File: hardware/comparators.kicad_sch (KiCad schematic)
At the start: 108 parts, among them J35 SMA, J36 SMA, J37 SMA, J38 SMA, J39 SMA, J40 SMA, J41 SMA, J42 SMA, J43 SMA, J44 SMA, J45 SMA, J46 SMA, J47 SMA, J48 SMA, J49 SMA, J50 SMA, J51 SMA, J52 SMA, J53 SMA, J54 SMA, J55 SMA, J56 SMA, J57 SMA, J58 SMA, SW7 SW_DIP_x03, U31 TXB0108PW, U32 TLV3502AIDR, U33 TLV3502AIDR, U34 TLV3502AIDR, U35 TLV3502AIDR, U36 TXB0108PW, U37 TLV3502AIDR, U38 TLV3502AIDR, U39 TLV3502AIDR, U40 TLV3502AIDR, U41 TXB0108PW, U42 TLV3502AIDR, U43 TLV3502AIDR, U44 TLV3502AIDR, U45 TLV3502AIDR

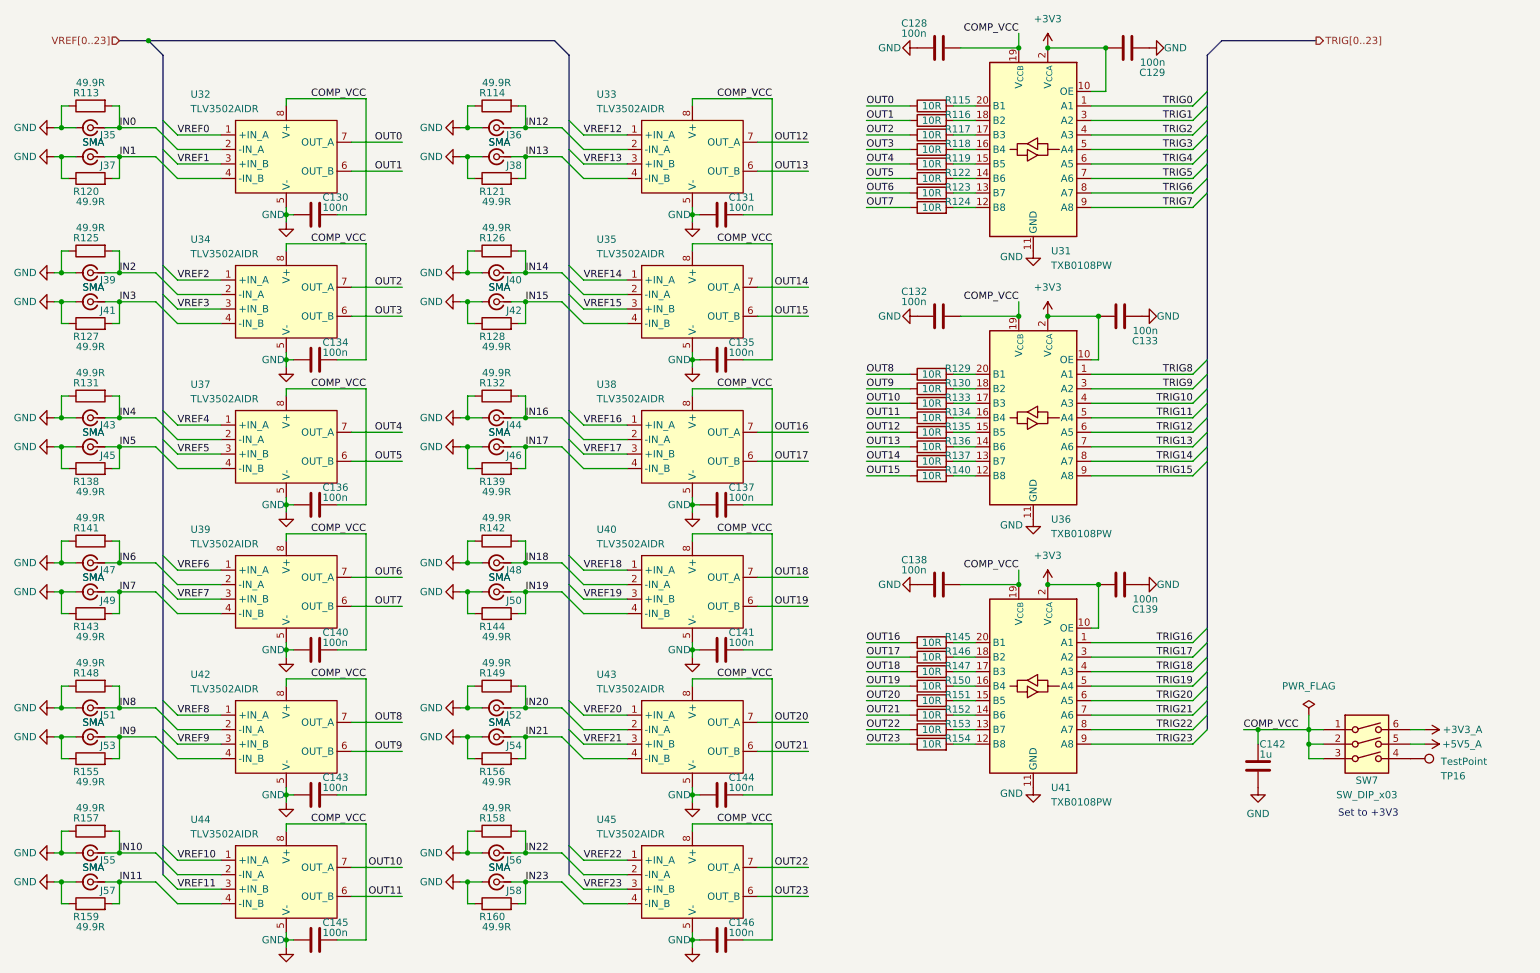
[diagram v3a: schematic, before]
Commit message: route digital inputs
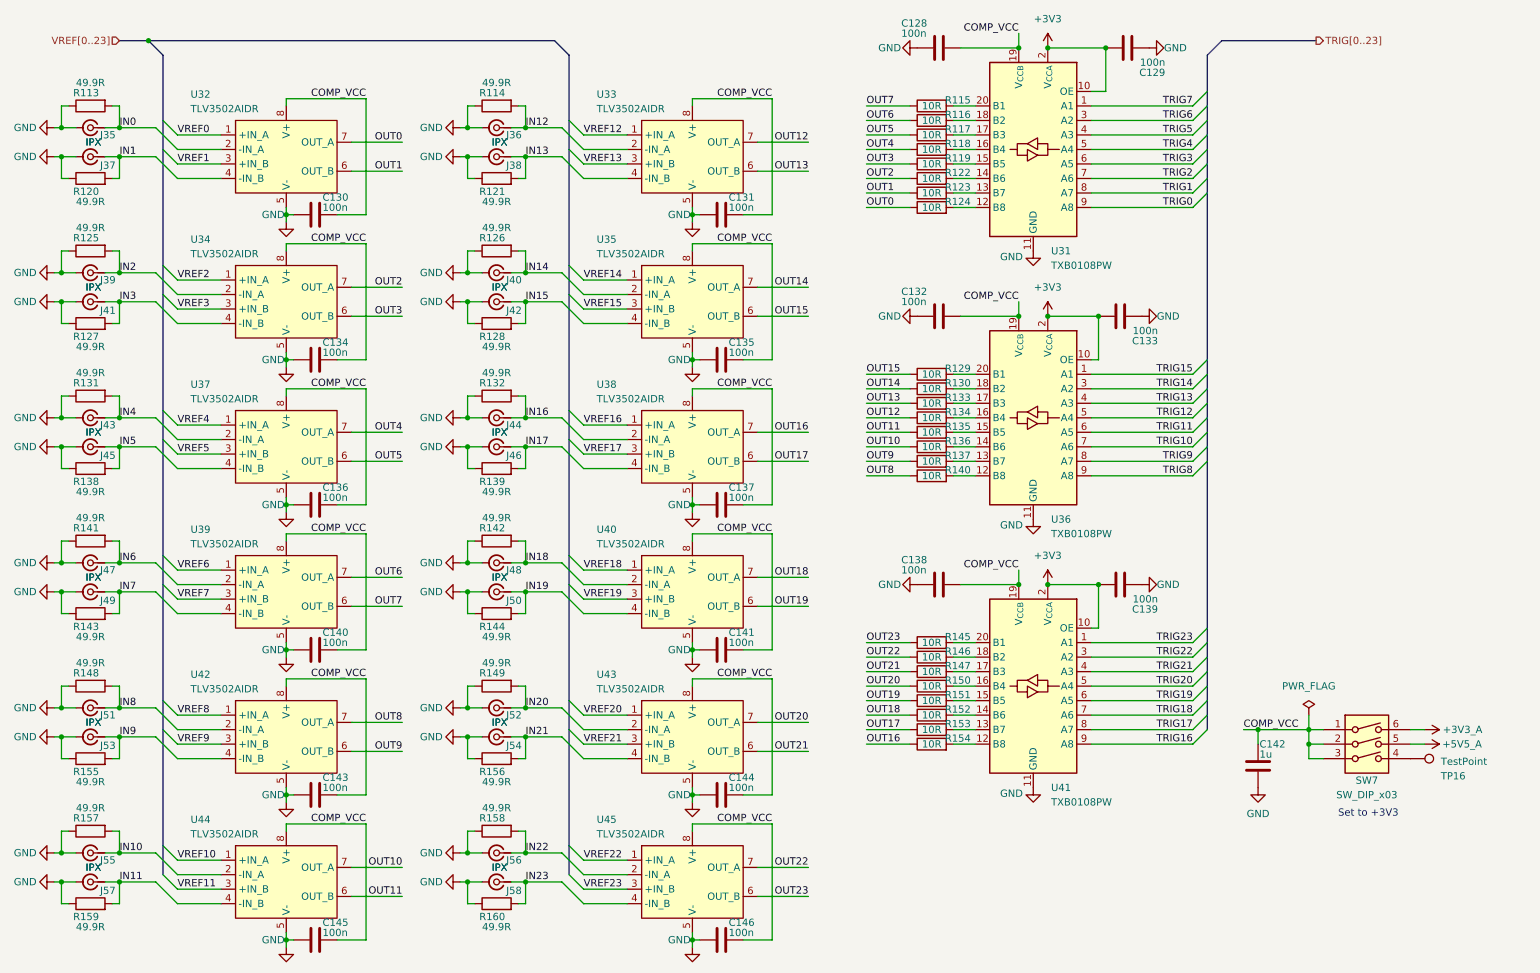
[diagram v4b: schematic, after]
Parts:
- J35, J36, J37, J38, J39, J40, J41, J42, J43, J44, J45, J46, J47, J48, J49, J50, J51, J52, J53, J54, J55, J56, J57, J58: value SMA -> IPX; footprint Connector_Coaxial:SMA_Amphenol_901-144_Vertical -> digital:BWIPX-1-001E
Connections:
- net OUT0: now also R124.1; no longer R115.1
- net OUT1: now also R123.1; no longer R116.1
- net OUT10: now also R136.1; no longer R133.1
- net OUT11: now also R135.1; no longer R134.1
- net OUT12: now also R134.1; no longer R135.1
- net OUT13: now also R133.1; no longer R136.1
- net OUT14: now also R130.1; no longer R137.1
- net OUT15: now also R129.1; no longer R140.1
- net OUT16: now also R154.1; no longer R145.1
- net OUT17: now also R153.1; no longer R146.1
- net OUT18: now also R152.1; no longer R147.1
- net OUT19: now also R151.1; no longer R150.1
- net OUT2: now also R122.1; no longer R117.1
- net OUT20: now also R150.1; no longer R151.1
- net OUT21: now also R147.1; no longer R152.1
- net OUT22: now also R146.1; no longer R153.1
- net OUT23: now also R145.1; no longer R154.1
- net OUT3: now also R119.1; no longer R118.1
- net OUT4: now also R118.1; no longer R119.1
- net OUT5: now also R117.1; no longer R122.1
- net OUT6: now also R116.1; no longer R123.1
- net OUT7: now also R115.1; no longer R124.1
- net OUT8: now also R140.1; no longer R129.1
- net OUT9: now also R137.1; no longer R130.1
- net TRIG0: now also U31.9 (A8); no longer U31.1 (A1)
- net TRIG1: now also U31.8 (A7); no longer U31.3 (A2)
- net TRIG10: now also U36.7 (A6); no longer U36.4 (A3)
- net TRIG11: now also U36.6 (A5); no longer U36.5 (A4)
- net TRIG12: now also U36.5 (A4); no longer U36.6 (A5)
- net TRIG13: now also U36.4 (A3); no longer U36.7 (A6)
- net TRIG14: now also U36.3 (A2); no longer U36.8 (A7)
- net TRIG15: now also U36.1 (A1); no longer U36.9 (A8)
- net TRIG16: now also U41.9 (A8); no longer U41.1 (A1)
- net TRIG17: now also U41.8 (A7); no longer U41.3 (A2)
- net TRIG18: now also U41.7 (A6); no longer U41.4 (A3)
- net TRIG19: now also U41.6 (A5); no longer U41.5 (A4)
- net TRIG2: now also U31.7 (A6); no longer U31.4 (A3)
- net TRIG20: now also U41.5 (A4); no longer U41.6 (A5)
- net TRIG21: now also U41.4 (A3); no longer U41.7 (A6)
- net TRIG22: now also U41.3 (A2); no longer U41.8 (A7)
- net TRIG23: now also U41.1 (A1); no longer U41.9 (A8)
- net TRIG3: now also U31.6 (A5); no longer U31.5 (A4)
- net TRIG4: now also U31.5 (A4); no longer U31.6 (A5)
- net TRIG5: now also U31.4 (A3); no longer U31.7 (A6)
- net TRIG6: now also U31.3 (A2); no longer U31.8 (A7)
- net TRIG7: now also U31.1 (A1); no longer U31.9 (A8)
- net TRIG8: now also U36.9 (A8); no longer U36.1 (A1)
- net TRIG9: now also U36.8 (A7); no longer U36.3 (A2)

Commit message: route more
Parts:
- removed TP16: TestPoint, TestPoint:TestPoint_Pad_D1.0mm, symbol Connector:TestPoint
- added TP17: TestPoint_Alt, digital:TestPoint_Keystone_5015_Micro_Mini, symbol Connector:TestPoint_Alt
- J35, J36, J37, J38, J39, J40, J41, J42, J43, J44, J45, J46, J47, J48, J49, J50, J51, J52, J53, J54, J55, J56, J57, J58: value IPX -> IPEX-1; LCSC (none) -> C496552
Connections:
- net at SW7.4: now also TP17.1

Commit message: route
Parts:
- renumbered C130 to C100, C131 to C101, C132 to C102, C133 to C103, C134 to C104, C135 to C105, C136 to C106, C137 to C107, C138 to C108, C139 to C109, C140 to C110, C141 to C111, C142 to C112, C143 to C113, C144 to C114, C145 to C115, C146 to C116, C128 to C98, C129 to C99, J35 to J21, J36 to J22, J37 to J23, J38 to J24, J39 to J25, J40 to J26, J41 to J27, J42 to J28, J43 to J29, J44 to J30, J45 to J31, J46 to J32, J47 to J33, J48 to J34, J49 to J35, J50 to J36, J51 to J37, J52 to J38, J53 to J39, J54 to J40, J55 to J41, J56 to J42, J57 to J43, J58 to J44, R124 to R100, R125 to R101, R126 to R102, R127 to R103, R128 to R104, R129 to R105, R130 to R106, R131 to R107, R132 to R108, R133 to R109, R134 to R110, R135 to R111, R136 to R112, R137 to R113, R138 to R114, R139 to R115, R140 to R116, R141 to R117, R142 to R118, R143 to R119, R144 to R120, R145 to R121, R146 to R122, R147 to R123, R148 to R124, R149 to R125, R150 to R126, R151 to R127, R152 to R128, R153 to R129, R154 to R130, R155 to R131, R156 to R132, R157 to R133, R158 to R134, R159 to R135, R160 to R136, R113 to R89, R114 to R90, R115 to R91, R116 to R92, R117 to R93, R118 to R94, R119 to R95, R120 to R96, R121 to R97, R122 to R98, R123 to R99, SW7 to SW6, TP17 to TP44, U31 to U24, U32 to U25, U33 to U26, U34 to U27, U35 to U28, U36 to U29, U37 to U30, U38 to U31, U39 to U32, U40 to U33, U41 to U34, U42 to U35, U43 to U36, U44 to U37, U45 to U38
